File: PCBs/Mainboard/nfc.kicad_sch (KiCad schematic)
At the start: 35 parts, among them IC2 ST25R3916-AQET, J4 NFC_ANTENNA, Y2 27.12MHz

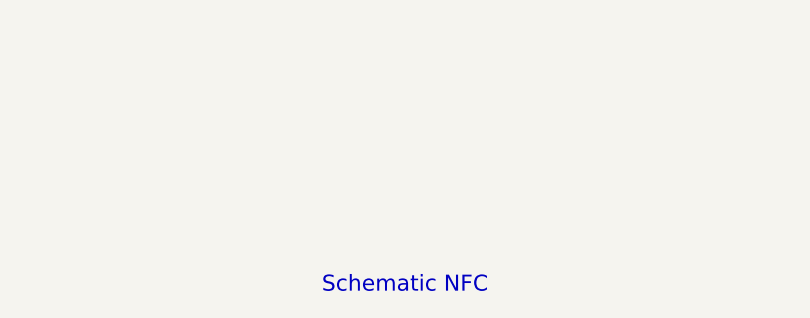
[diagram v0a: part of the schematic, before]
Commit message: Add progress report for 31.1.2025 Update relevant source files
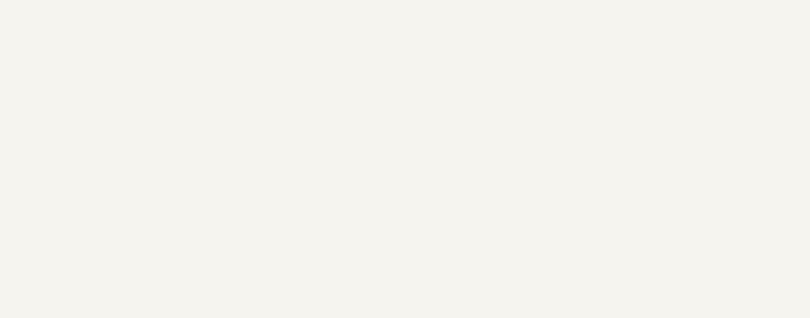
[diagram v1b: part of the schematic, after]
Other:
- note removed: "Schematic NFC"
- title: (none) -> NFC
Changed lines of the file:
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@@
 	(generator_version "8.0")
 	(paper "A4")
+	(title_block
+		(title "NFC")
+	)
 	(junction
 		(at 115.57 87.63)
@@
 		)
 	)
-	(text "Schematic NFC"
-		(exclude_from_sim no)
-		(at 196.85 189.992 0)
-		(effects
-			(font
-				(size 1.778 1.778)
-			)
-		)
-	)
 	(label "RFI2"
 		(at 110.49 71.12 180)
-		(fields_autoplaced yes)
 		(effects
 			(font
@@
 	(label "RFO2"
 		(at 162.56 88.9 0)
-		(fields_autoplaced yes)
 		(effects
 			(font
@@
 	(label "RFO1"
 		(at 162.56 58.42 0)
-		(fields_autoplaced yes)
 		(effects
 			(font
@@
 	(label "RFO2"
 		(at 110.49 63.5 180)
-		(fields_autoplaced yes)
 		(effects
 			(font
@@
 	(label "RFI1"
 		(at 110.49 74.93 180)
-		(fields_autoplaced yes)
 		(effects
 			(font
@@
 	(label "RFI2"
 		(at 162.56 95.25 0)
-		(fields_autoplaced yes)
 		(effects
 			(font
@@
 	(label "RFO1"
 		(at 110.49 67.31 180)
-		(fields_autoplaced yes)
 		(effects
 			(font
@@
 	(label "RFI1"
 		(at 162.56 52.07 0)
-		(fields_autoplaced yes)
 		(effects
 			(font
@@
 		(shape input)
 		(at 67.31 93.98 180)
-		(fields_autoplaced yes)
 		(effects
 			(font
@@
 		(shape input)
 		(at 67.31 86.36 180)
-		(fields_autoplaced yes)
 		(effects
 			(font
@@
 		(shape input)
 		(at 67.31 90.17 180)
-		(fields_autoplaced yes)
 		(effects
 			(font
